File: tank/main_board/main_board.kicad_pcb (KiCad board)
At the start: 2 copper layers, 59.7 x 72.4 mm, 45 parts, among them J1 PowerIn, J10 Sonar2, J11 Programming Header, J12 SigOut, J13 Conn_01x01, J14 Conn_01x01, J15 Conn_01x01, J16 PowerOut, J2 Conn_01x01, J3 Conn_01x01, J4 LED, J5 Conn_01x01, J6 Spk, J7 Hall2, J8 Hall1, J9 Sonar1, Q1 2N3904, U1 LM317_TO3, U2 ATMEGA328P-PU, U3 SN754410, U4 SN754410, Y1 Crystal

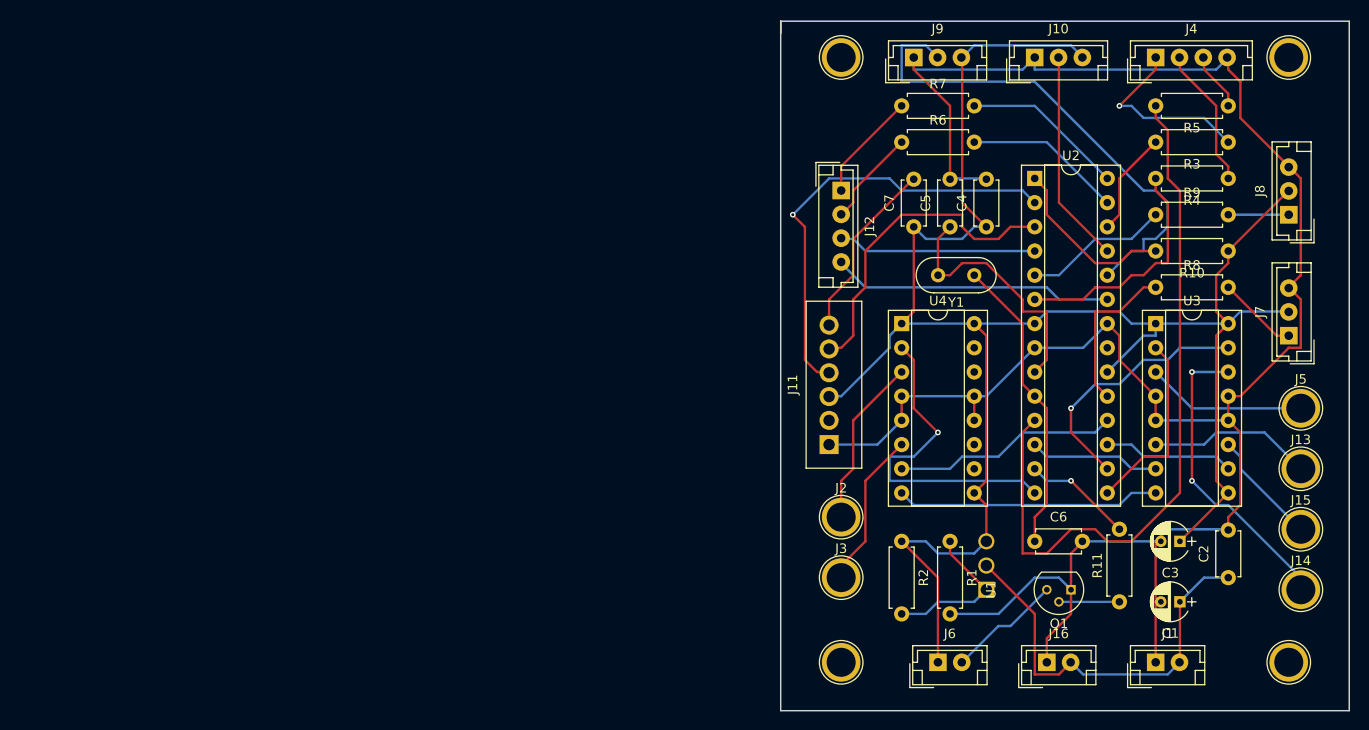
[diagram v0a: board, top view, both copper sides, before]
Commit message: Main Board v0.2
Adjustments to main board:
- resistors were inline when they shoulda been pull-ups
- adjust crystal footprint
- IR TX needs to be on pin 3
- silkscreen should have component names
- width of motor traces increased and added ground-fill
- motor vin isn't actually connected
- motor screw terminal footprints
- fix reset line - 1 uF cap
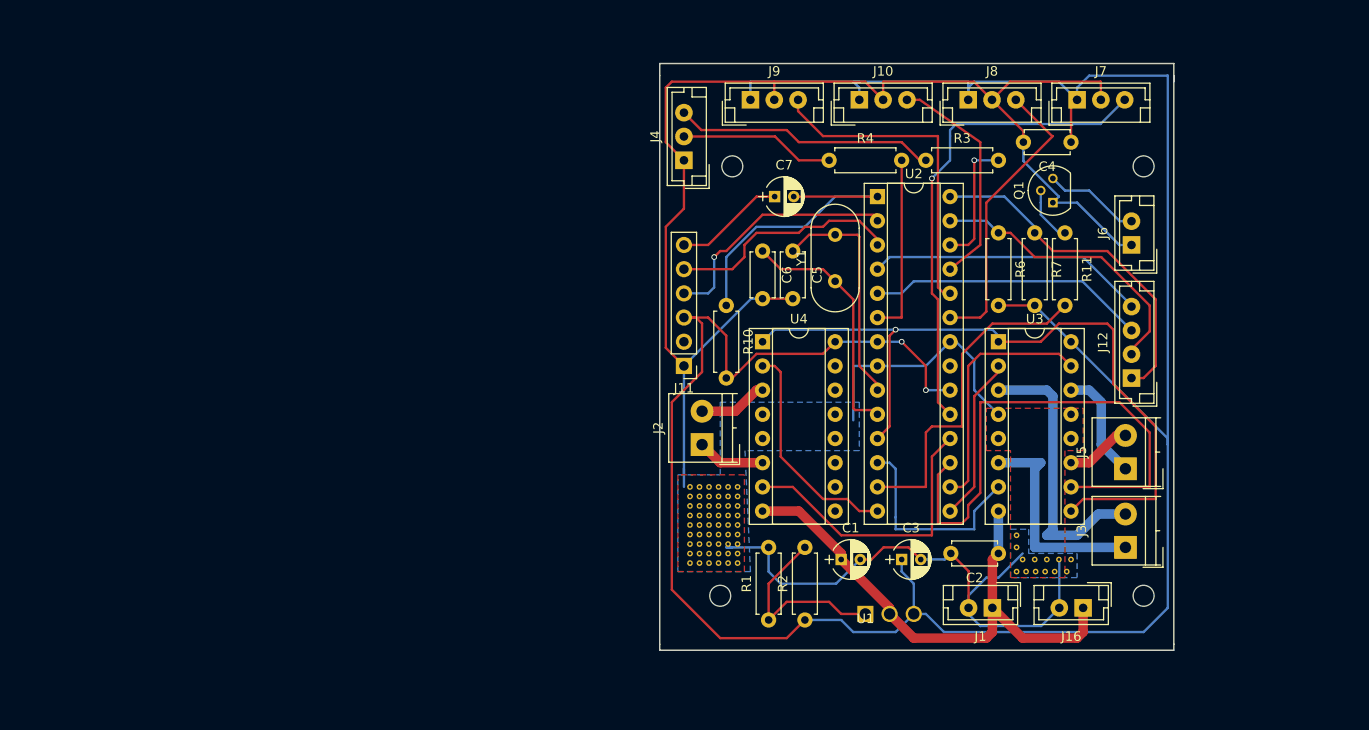
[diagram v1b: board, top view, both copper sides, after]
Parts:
- removed the G*** at (185.4, 130.8)
- removed J13, J14, J15: Conn_01x01, Connectors:1pin
- removed R5: R5, Resistors_THT:R_Axial_DIN0207_L6.3mm_D2.5mm_P7.62mm_Horizontal
- removed R8: R8, Resistors_THT:R_Axial_DIN0207_L6.3mm_D2.5mm_P7.62mm_Horizontal
- removed R9: R, Resistors_THT:R_Axial_DIN0207_L6.3mm_D2.5mm_P7.62mm_Horizontal
- removed the REF** at (176.5, 74.9)
- removed the REF** at (223.5, 74.9)
- removed the REF** at (223.5, 138.4)
- removed the REF** at (176.5, 138.4)
- added G***: LOGO, modules:miar_logo, B.Cu at (184.8, 113.0)
- added REF**: VIA-0.6mm, modules:VIA-0.6mm, F.Cu at (194.9, 126.4)
- added REF**: VIA-0.6mm, modules:VIA-0.6mm, F.Cu at (164.7, 127.0)
- added REF**: VIA-0.6mm, modules:VIA-0.6mm, F.Cu at (163.7, 127.0)
- added REF**: VIA-0.6mm, modules:VIA-0.6mm, F.Cu at (162.7, 127.0)
- added REF**: VIA-0.6mm, modules:VIA-0.6mm, F.Cu at (161.7, 127.0)
- added REF**: VIA-0.6mm, modules:VIA-0.6mm, F.Cu at (160.7, 127.0)
- added REF**: VIA-0.6mm, modules:VIA-0.6mm, F.Cu at (165.7, 126.0)
- added REF**: VIA-0.6mm, modules:VIA-0.6mm, F.Cu at (164.7, 126.0)
- added REF**: VIA-0.6mm, modules:VIA-0.6mm, F.Cu at (163.7, 126.0)
- added REF**: VIA-0.6mm, modules:VIA-0.6mm, F.Cu at (162.7, 126.0)
- added REF**: VIA-0.6mm, modules:VIA-0.6mm, F.Cu at (161.7, 126.0)
- added REF**: VIA-0.6mm, modules:VIA-0.6mm, F.Cu at (194.9, 125.1)
- added REF**: VIA-0.6mm, modules:VIA-0.6mm, F.Cu at (160.7, 126.0)
- added REF**: VIA-0.6mm, modules:VIA-0.6mm, F.Cu at (165.7, 125.0)
- added REF**: VIA-0.6mm, modules:VIA-0.6mm, F.Cu at (164.7, 125.0)
- added REF**: VIA-0.6mm, modules:VIA-0.6mm, F.Cu at (163.7, 125.0)
- added REF**: VIA-0.6mm, modules:VIA-0.6mm, F.Cu at (162.7, 125.0)
- added REF**: VIA-0.6mm, modules:VIA-0.6mm, F.Cu at (161.7, 125.0)
- added REF**: VIA-0.6mm, modules:VIA-0.6mm, F.Cu at (160.7, 125.0)
- added REF**: VIA-0.6mm, modules:VIA-0.6mm, F.Cu at (165.7, 124.0)
- added REF**: VIA-0.6mm, modules:VIA-0.6mm, F.Cu at (164.7, 124.0)
- added REF**: VIA-0.6mm, modules:VIA-0.6mm, F.Cu at (163.7, 124.0)
- added REF**: VIA-0.6mm, modules:VIA-0.6mm, F.Cu at (165.7, 128.0)
- added REF**: VIA-0.6mm, modules:VIA-0.6mm, F.Cu at (162.7, 124.0)
- added REF**: VIA-0.6mm, modules:VIA-0.6mm, F.Cu at (161.7, 124.0)
- added REF**: VIA-0.6mm, modules:VIA-0.6mm, F.Cu at (160.7, 124.0)
- added REF**: VIA-0.6mm, modules:VIA-0.6mm, F.Cu at (165.7, 123.0)
- added REF**: VIA-0.6mm, modules:VIA-0.6mm, F.Cu at (164.7, 123.0)
- added REF**: VIA-0.6mm, modules:VIA-0.6mm, F.Cu at (163.7, 123.0)
- added REF**: VIA-0.6mm, modules:VIA-0.6mm, F.Cu at (162.7, 123.0)
- added REF**: VIA-0.6mm, modules:VIA-0.6mm, F.Cu at (161.7, 123.0)
- added REF**: VIA-0.6mm, modules:VIA-0.6mm, F.Cu at (160.7, 123.0)
- added REF**: VIA-0.6mm, modules:VIA-0.6mm, F.Cu at (165.7, 122.0)
- added REF**: VIA-0.6mm, modules:VIA-0.6mm, F.Cu at (164.7, 128.0)
- added REF**: VIA-0.6mm, modules:VIA-0.6mm, F.Cu at (164.7, 122.0)
- added REF**: VIA-0.6mm, modules:VIA-0.6mm, F.Cu at (163.7, 122.0)
- added REF**: VIA-0.6mm, modules:VIA-0.6mm, F.Cu at (162.7, 122.0)
- added REF**: VIA-0.6mm, modules:VIA-0.6mm, F.Cu at (161.7, 122.0)
- added REF**: VIA-0.6mm, modules:VIA-0.6mm, F.Cu at (160.7, 122.0)
- added REF**: VIA-0.6mm, modules:VIA-0.6mm, F.Cu at (165.7, 121.0)
- added REF**: VIA-0.6mm, modules:VIA-0.6mm, F.Cu at (164.7, 121.0)
- added REF**: VIA-0.6mm, modules:VIA-0.6mm, F.Cu at (163.7, 121.0)
- added REF**: VIA-0.6mm, modules:VIA-0.6mm, F.Cu at (162.7, 121.0)
- added REF**: VIA-0.6mm, modules:VIA-0.6mm, F.Cu at (161.7, 121.0)
- added REF**: VIA-0.6mm, modules:VIA-0.6mm, F.Cu at (163.7, 128.0)
- added REF**: VIA-0.6mm, modules:VIA-0.6mm, F.Cu at (160.7, 121.0)
- added REF**: VIA-0.6mm, modules:VIA-0.6mm, F.Cu at (165.7, 120.0)
- added REF**: VIA-0.6mm, modules:VIA-0.6mm, F.Cu at (164.7, 120.0)
- added REF**: VIA-0.6mm, modules:VIA-0.6mm, F.Cu at (163.7, 120.0)
- added REF**: VIA-0.6mm, modules:VIA-0.6mm, F.Cu at (162.7, 120.0)
- added REF**: VIA-0.6mm, modules:VIA-0.6mm, F.Cu at (161.7, 120.0)
- added REF**: VIA-0.6mm, modules:VIA-0.6mm, F.Cu at (160.7, 120.0)
- added REF**: VIA-0.6mm, modules:VIA-0.6mm, F.Cu at (200.2, 128.9)
- added REF**: VIA-0.6mm, modules:VIA-0.6mm, F.Cu at (198.9, 128.9)
- added REF**: VIA-0.6mm, modules:VIA-0.6mm, F.Cu at (197.9, 128.9)
- added REF**: VIA-0.6mm, modules:VIA-0.6mm, F.Cu at (162.7, 128.0)
- added REF**: VIA-0.6mm, modules:VIA-0.6mm, F.Cu at (196.9, 128.9)
- added REF**: VIA-0.6mm, modules:VIA-0.6mm, F.Cu at (195.9, 128.9)
- added REF**: VIA-0.6mm, modules:VIA-0.6mm, F.Cu at (194.9, 128.9)
- added REF**: VIA-0.6mm, modules:VIA-0.6mm, F.Cu at (200.7, 127.6)
- added REF**: VIA-0.6mm, modules:VIA-0.6mm, F.Cu at (199.4, 127.6)
- added REF**: VIA-0.6mm, modules:VIA-0.6mm, F.Cu at (198.1, 127.6)
- added REF**: VIA-0.6mm, modules:VIA-0.6mm, F.Cu at (196.8, 127.6)
- added REF**: MountingHole_2.2mm_M2, Mounting_Holes:MountingHole_2.2mm_M2, F.Cu at (208.3, 131.4)
- added REF**: MountingHole_2.2mm_M2, Mounting_Holes:MountingHole_2.2mm_M2, F.Cu at (163.8, 131.4)
- added REF**: MountingHole_2.2mm_M2, Mounting_Holes:MountingHole_2.2mm_M2, F.Cu at (165.1, 86.4)
- added REF**: VIA-0.6mm, modules:VIA-0.6mm, F.Cu at (161.7, 128.0)
- added REF**: MountingHole_2.2mm_M2, Mounting_Holes:MountingHole_2.2mm_M2, F.Cu at (208.3, 86.4)
- added REF**: VIA-0.6mm, modules:VIA-0.6mm, F.Cu at (195.6, 127.6)
- added REF**: VIA-0.6mm, modules:VIA-0.6mm, F.Cu at (160.7, 128.0)
- added REF**: VIA-0.6mm, modules:VIA-0.6mm, F.Cu at (165.7, 127.0)
- C7: value C7 -> CP; footprint Capacitors_THT:C_Disc_D4.7mm_W2.5mm_P5.00mm -> Capacitors_THT:CP_Radial_D4.0mm_P2.00mm
- J1: value PowerIn -> Conn_01x02_Male
- J11: footprint Connectors:Wafer_Vertical17.5x5.8x7RM2.5-6 -> Pin_Headers:Pin_Header_Straight_1x06_Pitch2.54mm
- J2, J3, J5: value Conn_01x01 -> Conn_01x02; footprint Connectors:1pin -> Connectors_Terminal_Blocks:TerminalBlock_4UCON_19963_02x3.5mm_Straight
- J4: value LED -> Conn_01x03_Male; footprint JST:JST_EH_B04B-EH-A_04x2.50mm_Straight -> JST:JST_EH_B03B-EH-A_03x2.50mm_Straight
- Y1: footprint Crystals:Crystal_HC52-6mm_Vertical -> Crystals:Crystal_HC49-U_Vertical
- moved R10 53.0 mm to (164.5, 101.0), turned to 270 degrees
- moved J4 50.7 mm to (160.0, 85.7), turned to 90 degrees
- moved J6 48.3 mm to (207.0, 94.6), turned to 90 degrees
- moved R4 42.0 mm to (175.3, 85.7), turned to 0 degrees
- moved C6 41.8 mm to (168.3, 95.2), turned to 270 degrees
- moved Q1 40.7 mm to (198.8, 90.2), turned to 90 degrees
- moved R11 39.2 mm to (200.0, 93.3), turned to 270 degrees
- moved J12 36.3 mm to (207.0, 108.6), turned to 90 degrees
- moved C1 35.8 mm to (176.5, 127.6), turned to 0 degrees
- moved J8 35.8 mm to (189.9, 79.4), turned to 0 degrees
- moved J7 33.3 mm to (201.3, 79.4), turned to 0 degrees
- moved R3 31.8 mm to (185.4, 85.7), turned to 0 degrees
- moved J3 30.0 mm to (206.4, 126.4), turned to 90 degrees
- moved C3 29.3 mm to (182.9, 127.6), turned to 0 degrees
- moved C2 24.3 mm to (193.0, 127.0), turned to 180 degrees
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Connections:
- net LED2 renamed LED0
- net Speaker renamed SPK
- C1 pad 1: Net-(C1-Pad1) -> 5V
- C2 pad 1: Net-(C1-Pad1) -> 5V
- C7 pad 1: 4.5V -> Net-(C7-Pad1)
- J1 pad 1: GND -> 5V
- J1 pad 2: Net-(C1-Pad1) -> GND
- J10 pad 1: GND -> 4.5V
- J10 pad 2: Sonar2 -> GND
- J10 pad 3: 4.5V -> Net-(J10-Pad3)
- J11 pad 4: Net-(J11-Pad4) -> Rx
- J11 pad 5: Net-(J11-Pad5) -> Tx
- J11 pad 6: Net-(C7-Pad2) -> Net-(C7-Pad1)
- J12 pad 1: SLC -> SCL
- J12 pad 3: Rx -> IRTx
- J12 pad 4: Tx -> IRRx
- J16 pad 1: GND -> 5V
- J16 pad 2: Net-(C1-Pad1) -> GND
- J4 pad 1: Net-(J4-Pad1) -> GND
- J6 pad 1: 4.5V -> GND
- J7 pad 1: TurretCal -> 4.5V
- J7 pad 2: 4.5V -> GND
- J7 pad 3: GND -> Net-(J7-Pad3)
- J8 pad 1: TurretEnc -> 4.5V
- J8 pad 2: 4.5V -> GND
- J8 pad 3: GND -> Net-(J8-Pad3)
- J9 pad 1: GND -> 4.5V
- J9 pad 2: Sonar1 -> GND
- J9 pad 3: 4.5V -> Net-(J9-Pad3)
- R10 pad 1: 4.5V -> Net-(C7-Pad2)
- R10 pad 2: Net-(R10-Pad2) -> 4.5V
- R3 pad 1: Net-(J4-Pad1) -> Net-(J4-Pad3)
- R6 pad 2: Net-(R6-Pad2) -> 4.5V
- R7 pad 1: SLC -> SCL
- R7 pad 2: Net-(R7-Pad2) -> 4.5V
- U1 pad 2: Net-(C1-Pad1) -> 5V
- U2 pad 1: Net-(R10-Pad2) -> Net-(C7-Pad2)
- U2 pad 11: LED3 -> MEnable
- U2 pad 19: Net-(R8-Pad1) -> Net-(J7-Pad3)
- U2 pad 2: Net-(J11-Pad4) -> Rx
- U2 pad 23: Tx -> Net-(J8-Pad3)
- U2 pad 24: Sonar1 -> Net-(J9-Pad3)
- U2 pad 25: Sonar2 -> Net-(J10-Pad3)
- U2 pad 27: Net-(R6-Pad2) -> SDA
- U2 pad 28: Net-(R7-Pad2) -> SCL
- U2 pad 3: Net-(J11-Pad5) -> Tx
- U2 pad 4: Rx -> IRRx
- U2 pad 5: Net-(R9-Pad1) -> IRTx
- U3 pad 1: 4.5V -> MEnable
- U3 pad 11: Net-(J15-Pad1) -> Net-(J5-Pad2)
- U3 pad 14: Net-(J14-Pad1) -> Net-(J5-Pad1)
- U3 pad 3: Net-(J5-Pad1) -> Net-(J3-Pad2)
- U3 pad 6: Net-(J13-Pad1) -> Net-(J3-Pad1)
- U3 pad 9: 4.5V -> MEnable
- U4 pad 1: 4.5V -> MEnable
- U4 pad 3: Net-(J2-Pad1) -> Net-(J2-Pad2)
- U4 pad 6: Net-(J3-Pad1) -> Net-(J2-Pad1)
- U4 pad 9: 4.5V -> Net-(U4-Pad9)
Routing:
- net MEnable: track 0.00 -> 80.6 mm, vias 0 -> 1
- net LED3: track 76.4 -> 0.00 mm
- net 4.5V: track 206.3 -> 275.0 mm, vias 0 -> 2
- net Sonar1: track 53.1 -> 0.00 mm
- net Net-(J7-Pad3): track 0.00 -> 51.1 mm, vias 0 -> 1
- net Net-(J11-Pad4): track 46.9 -> 0.00 mm, vias 1 -> 0
- net Net-(C1-Pad1): track 43.0 -> 0.00 mm
- net M1-: track 13.8 -> 56.0 mm
- net SCL: track 0.00 -> 36.5 mm
- net Net-(J9-Pad3): track 0.00 -> 34.4 mm
- net Net-(J11-Pad5): track 34.3 -> 0.00 mm
- net Net-(J14-Pad1): track 32.1 -> 0.00 mm, vias 2 -> 0
- net Net-(J8-Pad3): track 0.00 -> 30.8 mm
- net IRTx: track 0.00 -> 30.5 mm
- net Net-(J3-Pad2): track 0.00 -> 30.0 mm
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- added copper zone on B.Cu, net GND
- added copper zone on F.Cu, net GND
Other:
- board size 59.7 x 72.4 mm -> 54 x 61.6 mm
- net class Motor: clearance 0.4 -> 0.2; trace_width 0.5 -> 1
- board text added: "Laser Tag Robot Tank Main Board v0.2 M.I.A.R. Labs nick.groesz@gmail.com"
- board text removed: "Tank Main Board v0.1 M.I.A.R Labs nick.groesz@gmail.com"

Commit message: Main Board v0.3 - changed motor controllers to TB6612FNG - changed speaker transistor wiring - supports 4 LEDs, using switched ground
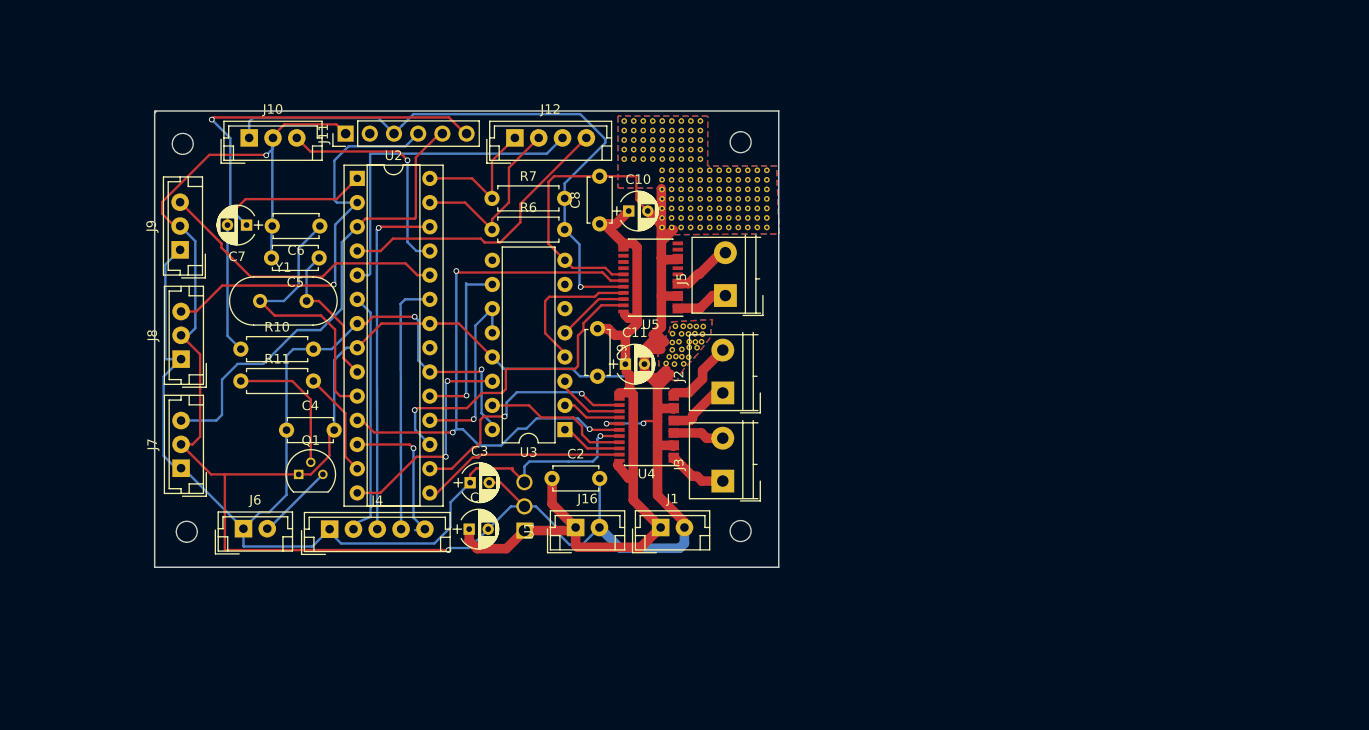
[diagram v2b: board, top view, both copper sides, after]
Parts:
- removed the G*** at (184.8, 113.0)
- removed R1: R1, Resistors_THT:R_Axial_DIN0207_L6.3mm_D2.5mm_P7.62mm_Horizontal
- removed R2: R2, Resistors_THT:R_Axial_DIN0207_L6.3mm_D2.5mm_P7.62mm_Horizontal
- removed R3: R3, Resistors_THT:R_Axial_DIN0207_L6.3mm_D2.5mm_P7.62mm_Horizontal
- removed R4: R4, Resistors_THT:R_Axial_DIN0207_L6.3mm_D2.5mm_P7.62mm_Horizontal
- removed the REF** at (194.9, 126.4)
- removed the REF** at (164.7, 127.0)
- removed the REF** at (163.7, 127.0)
- removed the REF** at (162.7, 127.0)
- removed the REF** at (161.7, 127.0)
- removed the REF** at (160.7, 127.0)
- removed the REF** at (165.7, 126.0)
- removed the REF** at (164.7, 126.0)
- removed the REF** at (163.7, 126.0)
- removed the REF** at (162.7, 126.0)
- removed the REF** at (161.7, 126.0)
- removed the REF** at (194.9, 125.1)
- removed the REF** at (160.7, 126.0)
- removed the REF** at (165.7, 125.0)
- removed the REF** at (164.7, 125.0)
- removed the REF** at (163.7, 125.0)
- removed the REF** at (162.7, 125.0)
- removed the REF** at (161.7, 125.0)
- removed the REF** at (160.7, 125.0)
- removed the REF** at (165.7, 124.0)
- removed the REF** at (164.7, 124.0)
- removed the REF** at (163.7, 124.0)
- removed the REF** at (165.7, 128.0)
- removed the REF** at (162.7, 124.0)
- removed the REF** at (161.7, 124.0)
- removed the REF** at (160.7, 124.0)
- removed the REF** at (165.7, 123.0)
- removed the REF** at (164.7, 123.0)
- removed the REF** at (163.7, 123.0)
- removed the REF** at (162.7, 123.0)
- removed the REF** at (161.7, 123.0)
- removed the REF** at (160.7, 123.0)
- removed the REF** at (165.7, 122.0)
- removed the REF** at (164.7, 128.0)
- removed the REF** at (164.7, 122.0)
- removed the REF** at (163.7, 122.0)
- removed the REF** at (162.7, 122.0)
- removed the REF** at (161.7, 122.0)
- removed the REF** at (160.7, 122.0)
- removed the REF** at (165.7, 121.0)
- removed the REF** at (164.7, 121.0)
- removed the REF** at (163.7, 121.0)
- removed the REF** at (162.7, 121.0)
- removed the REF** at (161.7, 121.0)
- removed the REF** at (163.7, 128.0)
- removed the REF** at (160.7, 121.0)
- removed the REF** at (165.7, 120.0)
- removed the REF** at (164.7, 120.0)
- removed the REF** at (163.7, 120.0)
- removed the REF** at (162.7, 120.0)
- removed the REF** at (161.7, 120.0)
- removed the REF** at (160.7, 120.0)
- removed the REF** at (200.2, 128.9)
- removed the REF** at (198.9, 128.9)
- removed the REF** at (197.9, 128.9)
- removed the REF** at (162.7, 128.0)
- removed the REF** at (196.9, 128.9)
- removed the REF** at (195.9, 128.9)
- removed the REF** at (194.9, 128.9)
- removed the REF** at (200.7, 127.6)
- removed the REF** at (199.4, 127.6)
- removed the REF** at (198.1, 127.6)
- removed the REF** at (196.8, 127.6)
- removed the REF** at (208.3, 131.4)
- removed the REF** at (163.8, 131.4)
- removed the REF** at (165.1, 86.4)
- removed the REF** at (161.7, 128.0)
- removed the REF** at (208.3, 86.4)
- removed the REF** at (195.6, 127.6)
- removed the REF** at (160.7, 128.0)
- removed the REF** at (165.7, 127.0)
- added C10: CP, Capacitors_THT:CP_Radial_D4.0mm_P2.00mm, F.Cu at (154.2, 91.0)
- added C11: CP, Capacitors_THT:CP_Radial_D4.0mm_P2.00mm, F.Cu at (153.9, 107.1)
- added C8: C, Capacitors_THT:C_Disc_D4.7mm_W2.5mm_P5.00mm, F.Cu at (151.2, 92.4)
- added C9: C, Capacitors_THT:C_Disc_D4.7mm_W2.5mm_P5.00mm, F.Cu at (150.9, 103.4)
- added G***: LOGO, modules:Tank, B.Cu at (129.2, 115.0)
- added REF**: VIA-0.6mm, modules:VIA-0.6mm, F.Cu at (158.2, 107.0)
- added REF**: VIA-0.6mm, modules:VIA-0.6mm, F.Cu at (160.6, 105.4)
- added REF**: VIA-0.6mm, modules:VIA-0.6mm, F.Cu at (166.7, 86.8)
- added REF**: VIA-0.6mm, modules:VIA-0.6mm, F.Cu at (165.7, 86.8)
- added REF**: VIA-0.6mm, modules:VIA-0.6mm, F.Cu at (164.7, 86.8)
- added REF**: VIA-0.6mm, modules:VIA-0.6mm, F.Cu at (163.7, 86.8)
- added REF**: VIA-0.6mm, modules:VIA-0.6mm, F.Cu at (162.7, 86.8)
- added REF**: VIA-0.6mm, modules:VIA-0.6mm, F.Cu at (161.7, 86.8)
- added REF**: VIA-0.6mm, modules:VIA-0.6mm, F.Cu at (160.7, 86.8)
- added REF**: VIA-0.6mm, modules:VIA-0.6mm, F.Cu at (159.7, 86.8)
- added REF**: VIA-0.6mm, modules:VIA-0.6mm, F.Cu at (158.7, 86.8)
- added REF**: VIA-0.6mm, modules:VIA-0.6mm, F.Cu at (157.7, 86.8)
- added REF**: VIA-0.6mm, modules:VIA-0.6mm, F.Cu at (161.4, 105.4)
- added REF**: VIA-0.6mm, modules:VIA-0.6mm, F.Cu at (161.8, 85.6)
- added REF**: VIA-0.6mm, modules:VIA-0.6mm, F.Cu at (160.8, 85.6)
- added REF**: VIA-0.6mm, modules:VIA-0.6mm, F.Cu at (159.8, 85.6)
- added REF**: VIA-0.6mm, modules:VIA-0.6mm, F.Cu at (158.8, 85.6)
- added REF**: VIA-0.6mm, modules:VIA-0.6mm, F.Cu at (157.8, 85.6)
- added REF**: VIA-0.6mm, modules:VIA-0.6mm, F.Cu at (156.8, 85.6)
- added REF**: VIA-0.6mm, modules:VIA-0.6mm, F.Cu at (155.8, 85.6)
- added REF**: VIA-0.6mm, modules:VIA-0.6mm, F.Cu at (154.8, 85.6)
- added REF**: VIA-0.6mm, modules:VIA-0.6mm, F.Cu at (153.8, 85.6)
- added REF**: VIA-0.6mm, modules:VIA-0.6mm, F.Cu at (161.8, 84.6)
- added REF**: VIA-0.6mm, modules:VIA-0.6mm, F.Cu at (161.9, 104.8)
- added REF**: VIA-0.6mm, modules:VIA-0.6mm, F.Cu at (160.8, 84.6)
- added REF**: VIA-0.6mm, modules:VIA-0.6mm, F.Cu at (159.8, 84.6)
- added REF**: VIA-0.6mm, modules:VIA-0.6mm, F.Cu at (158.8, 84.6)
- added REF**: VIA-0.6mm, modules:VIA-0.6mm, F.Cu at (157.8, 84.6)
- added REF**: VIA-0.6mm, modules:VIA-0.6mm, F.Cu at (156.8, 84.6)
- added REF**: VIA-0.6mm, modules:VIA-0.6mm, F.Cu at (155.8, 84.6)
- added REF**: VIA-0.6mm, modules:VIA-0.6mm, F.Cu at (154.8, 84.6)
- added REF**: VIA-0.6mm, modules:VIA-0.6mm, F.Cu at (153.8, 84.6)
- added REF**: VIA-0.6mm, modules:VIA-0.6mm, F.Cu at (161.8, 83.6)
- added REF**: VIA-0.6mm, modules:VIA-0.6mm, F.Cu at (160.8, 83.6)
- added REF**: VIA-0.6mm, modules:VIA-0.6mm, F.Cu at (161.2, 104.8)
- added REF**: VIA-0.6mm, modules:VIA-0.6mm, F.Cu at (159.8, 83.6)
- added REF**: VIA-0.6mm, modules:VIA-0.6mm, F.Cu at (158.8, 83.6)
- added REF**: VIA-0.6mm, modules:VIA-0.6mm, F.Cu at (157.8, 83.6)
- added REF**: VIA-0.6mm, modules:VIA-0.6mm, F.Cu at (156.8, 83.6)
- added REF**: VIA-0.6mm, modules:VIA-0.6mm, F.Cu at (155.8, 83.6)
- added REF**: VIA-0.6mm, modules:VIA-0.6mm, F.Cu at (154.8, 83.6)
- added REF**: VIA-0.6mm, modules:VIA-0.6mm, F.Cu at (153.8, 83.6)
- added REF**: VIA-0.6mm, modules:VIA-0.6mm, F.Cu at (161.8, 82.6)
- added REF**: VIA-0.6mm, modules:VIA-0.6mm, F.Cu at (160.8, 82.6)
- added REF**: VIA-0.6mm, modules:VIA-0.6mm, F.Cu at (159.8, 82.6)
- added REF**: VIA-0.6mm, modules:VIA-0.6mm, F.Cu at (160.6, 104.8)
- added REF**: VIA-0.6mm, modules:VIA-0.6mm, F.Cu at (158.8, 82.6)
- added REF**: VIA-0.6mm, modules:VIA-0.6mm, F.Cu at (157.8, 82.6)
- added REF**: VIA-0.6mm, modules:VIA-0.6mm, F.Cu at (156.8, 82.6)
- added REF**: VIA-0.6mm, modules:VIA-0.6mm, F.Cu at (155.8, 82.6)
- added REF**: VIA-0.6mm, modules:VIA-0.6mm, F.Cu at (154.8, 82.6)
- added REF**: VIA-0.6mm, modules:VIA-0.6mm, F.Cu at (153.8, 82.6)
- added REF**: VIA-0.6mm, modules:VIA-0.6mm, F.Cu at (161.8, 81.6)
- added REF**: VIA-0.6mm, modules:VIA-0.6mm, F.Cu at (160.8, 81.6)
- added REF**: VIA-0.6mm, modules:VIA-0.6mm, F.Cu at (159.8, 81.6)
- added REF**: VIA-0.6mm, modules:VIA-0.6mm, F.Cu at (158.8, 81.6)
- added REF**: VIA-0.6mm, modules:VIA-0.6mm, F.Cu at (159.5, 104.8)
- added REF**: VIA-0.6mm, modules:VIA-0.6mm, F.Cu at (157.8, 81.6)
- added REF**: VIA-0.6mm, modules:VIA-0.6mm, F.Cu at (156.8, 81.6)
- added REF**: VIA-0.6mm, modules:VIA-0.6mm, F.Cu at (155.8, 81.6)
- added REF**: VIA-0.6mm, modules:VIA-0.6mm, F.Cu at (154.8, 81.6)
- added REF**: MountingHole_2.2mm_M2, Mounting_Holes:MountingHole_2.2mm_M2, F.Cu at (107.8, 124.7)
- added REF**: MountingHole_2.2mm_M2, Mounting_Holes:MountingHole_2.2mm_M2, F.Cu at (107.4, 84.0)
- added REF**: MountingHole_2.2mm_M2, Mounting_Holes:MountingHole_2.2mm_M2, F.Cu at (166.0, 83.8)
- added REF**: MountingHole_2.2mm_M2, Mounting_Holes:MountingHole_2.2mm_M2, F.Cu at (166.0, 124.7)
- added REF**: VIA-0.6mm, modules:VIA-0.6mm, F.Cu at (153.8, 81.6)
- added REF**: VIA-0.6mm, modules:VIA-0.6mm, F.Cu at (159.1, 103.2)
- added REF**: VIA-0.6mm, modules:VIA-0.6mm, F.Cu at (158.8, 104.8)
- added REF**: VIA-0.6mm, modules:VIA-0.6mm, F.Cu at (158.8, 103.9)
- added REF**: VIA-0.6mm, modules:VIA-0.6mm, F.Cu at (159.8, 104.0)
- added REF**: VIA-0.6mm, modules:VIA-0.6mm, F.Cu at (160.5, 104.0)
- added REF**: VIA-0.6mm, modules:VIA-0.6mm, F.Cu at (159.0, 107.1)
- added REF**: VIA-0.6mm, modules:VIA-0.6mm, F.Cu at (161.2, 103.9)
- added REF**: VIA-0.6mm, modules:VIA-0.6mm, F.Cu at (162.0, 104.0)
- added REF**: VIA-0.6mm, modules:VIA-0.6mm, F.Cu at (162.1, 103.2)
- added REF**: VIA-0.6mm, modules:VIA-0.6mm, F.Cu at (161.3, 103.2)
- added REF**: VIA-0.6mm, modules:VIA-0.6mm, F.Cu at (160.7, 103.2)
- added REF**: VIA-0.6mm, modules:VIA-0.6mm, F.Cu at (159.9, 103.2)
- added REF**: VIA-0.6mm, modules:VIA-0.6mm, F.Cu at (168.7, 92.8)
- added REF**: VIA-0.6mm, modules:VIA-0.6mm, F.Cu at (167.7, 92.8)
- added REF**: VIA-0.6mm, modules:VIA-0.6mm, F.Cu at (166.7, 92.8)
- added REF**: VIA-0.6mm, modules:VIA-0.6mm, F.Cu at (165.7, 92.8)
- added REF**: VIA-0.6mm, modules:VIA-0.6mm, F.Cu at (160.0, 107.1)
- added REF**: VIA-0.6mm, modules:VIA-0.6mm, F.Cu at (164.7, 92.8)
- added REF**: VIA-0.6mm, modules:VIA-0.6mm, F.Cu at (163.7, 92.8)
- added REF**: VIA-0.6mm, modules:VIA-0.6mm, F.Cu at (162.7, 92.8)
- added REF**: VIA-0.6mm, modules:VIA-0.6mm, F.Cu at (161.7, 92.8)
- added REF**: VIA-0.6mm, modules:VIA-0.6mm, F.Cu at (160.7, 92.8)
- added REF**: VIA-0.6mm, modules:VIA-0.6mm, F.Cu at (159.7, 92.8)
- added REF**: VIA-0.6mm, modules:VIA-0.6mm, F.Cu at (158.7, 92.8)
- added REF**: VIA-0.6mm, modules:VIA-0.6mm, F.Cu at (157.7, 92.8)
- added REF**: VIA-0.6mm, modules:VIA-0.6mm, F.Cu at (168.7, 91.8)
- added REF**: VIA-0.6mm, modules:VIA-0.6mm, F.Cu at (167.7, 91.8)
- added REF**: VIA-0.6mm, modules:VIA-0.6mm, F.Cu at (160.5, 106.4)
- added REF**: VIA-0.6mm, modules:VIA-0.6mm, F.Cu at (166.7, 91.8)
- added REF**: VIA-0.6mm, modules:VIA-0.6mm, F.Cu at (165.7, 91.8)
- added REF**: VIA-0.6mm, modules:VIA-0.6mm, F.Cu at (164.7, 91.8)
- added REF**: VIA-0.6mm, modules:VIA-0.6mm, F.Cu at (163.7, 91.8)
- added REF**: VIA-0.6mm, modules:VIA-0.6mm, F.Cu at (162.7, 91.8)
- added REF**: VIA-0.6mm, modules:VIA-0.6mm, F.Cu at (161.7, 91.8)
- added REF**: VIA-0.6mm, modules:VIA-0.6mm, F.Cu at (160.7, 91.8)
- added REF**: VIA-0.6mm, modules:VIA-0.6mm, F.Cu at (159.7, 91.8)
- added REF**: VIA-0.6mm, modules:VIA-0.6mm, F.Cu at (158.7, 91.8)
- added REF**: VIA-0.6mm, modules:VIA-0.6mm, F.Cu at (157.7, 91.8)
- added REF**: VIA-0.6mm, modules:VIA-0.6mm, F.Cu at (159.8, 106.3)
- added REF**: VIA-0.6mm, modules:VIA-0.6mm, F.Cu at (168.7, 90.8)
- added REF**: VIA-0.6mm, modules:VIA-0.6mm, F.Cu at (167.7, 90.8)
- added REF**: VIA-0.6mm, modules:VIA-0.6mm, F.Cu at (166.7, 90.8)
- added REF**: VIA-0.6mm, modules:VIA-0.6mm, F.Cu at (165.7, 90.8)
- added REF**: VIA-0.6mm, modules:VIA-0.6mm, F.Cu at (164.7, 90.8)
- added REF**: VIA-0.6mm, modules:VIA-0.6mm, F.Cu at (163.7, 90.8)
- added REF**: VIA-0.6mm, modules:VIA-0.6mm, F.Cu at (162.7, 90.8)
- added REF**: VIA-0.6mm, modules:VIA-0.6mm, F.Cu at (161.7, 90.8)
- added REF**: VIA-0.6mm, modules:VIA-0.6mm, F.Cu at (160.7, 90.8)
- added REF**: VIA-0.6mm, modules:VIA-0.6mm, F.Cu at (159.7, 90.8)
- added REF**: VIA-0.6mm, modules:VIA-0.6mm, F.Cu at (159.2, 106.3)
- added REF**: VIA-0.6mm, modules:VIA-0.6mm, F.Cu at (158.7, 90.8)
- added REF**: VIA-0.6mm, modules:VIA-0.6mm, F.Cu at (157.7, 90.8)
- added REF**: VIA-0.6mm, modules:VIA-0.6mm, F.Cu at (168.7, 89.8)
- added REF**: VIA-0.6mm, modules:VIA-0.6mm, F.Cu at (167.7, 89.8)
- added REF**: VIA-0.6mm, modules:VIA-0.6mm, F.Cu at (166.7, 89.8)
- added REF**: VIA-0.6mm, modules:VIA-0.6mm, F.Cu at (165.7, 89.8)
- added REF**: VIA-0.6mm, modules:VIA-0.6mm, F.Cu at (164.7, 89.8)
- added REF**: VIA-0.6mm, modules:VIA-0.6mm, F.Cu at (163.7, 89.8)
- added REF**: VIA-0.6mm, modules:VIA-0.6mm, F.Cu at (162.7, 89.8)
- added REF**: VIA-0.6mm, modules:VIA-0.6mm, F.Cu at (161.7, 89.8)
- added REF**: VIA-0.6mm, modules:VIA-0.6mm, F.Cu at (158.5, 106.3)
- added REF**: VIA-0.6mm, modules:VIA-0.6mm, F.Cu at (160.7, 89.8)
- added REF**: VIA-0.6mm, modules:VIA-0.6mm, F.Cu at (159.7, 89.8)
- added REF**: VIA-0.6mm, modules:VIA-0.6mm, F.Cu at (158.7, 89.8)
- added REF**: VIA-0.6mm, modules:VIA-0.6mm, F.Cu at (157.7, 89.8)
- added REF**: VIA-0.6mm, modules:VIA-0.6mm, F.Cu at (168.7, 88.8)
- added REF**: VIA-0.6mm, modules:VIA-0.6mm, F.Cu at (167.7, 88.8)
- added REF**: VIA-0.6mm, modules:VIA-0.6mm, F.Cu at (166.7, 88.8)
- added REF**: VIA-0.6mm, modules:VIA-0.6mm, F.Cu at (165.7, 88.8)
- added REF**: VIA-0.6mm, modules:VIA-0.6mm, F.Cu at (164.7, 88.8)
- added REF**: VIA-0.6mm, modules:VIA-0.6mm, F.Cu at (163.7, 88.8)
- added REF**: VIA-0.6mm, modules:VIA-0.6mm, F.Cu at (158.8, 105.6)
- added REF**: VIA-0.6mm, modules:VIA-0.6mm, F.Cu at (162.7, 88.8)
- added REF**: VIA-0.6mm, modules:VIA-0.6mm, F.Cu at (161.7, 88.8)
- added REF**: VIA-0.6mm, modules:VIA-0.6mm, F.Cu at (160.7, 88.8)
- added REF**: VIA-0.6mm, modules:VIA-0.6mm, F.Cu at (159.7, 88.8)
- added REF**: VIA-0.6mm, modules:VIA-0.6mm, F.Cu at (158.7, 88.8)
- added REF**: VIA-0.6mm, modules:VIA-0.6mm, F.Cu at (157.7, 88.8)
- added REF**: VIA-0.6mm, modules:VIA-0.6mm, F.Cu at (168.7, 87.8)
- added REF**: VIA-0.6mm, modules:VIA-0.6mm, F.Cu at (167.7, 87.8)
- added REF**: VIA-0.6mm, modules:VIA-0.6mm, F.Cu at (166.7, 87.8)
- added REF**: VIA-0.6mm, modules:VIA-0.6mm, F.Cu at (165.7, 87.8)
- added REF**: VIA-0.6mm, modules:VIA-0.6mm, F.Cu at (159.8, 105.6)
- added REF**: VIA-0.6mm, modules:VIA-0.6mm, F.Cu at (164.7, 87.8)
- added REF**: VIA-0.6mm, modules:VIA-0.6mm, F.Cu at (163.7, 87.8)
- added REF**: VIA-0.6mm, modules:VIA-0.6mm, F.Cu at (162.7, 87.8)
- added REF**: VIA-0.6mm, modules:VIA-0.6mm, F.Cu at (161.7, 87.8)
- added REF**: VIA-0.6mm, modules:VIA-0.6mm, F.Cu at (160.7, 87.8)
- added REF**: VIA-0.6mm, modules:VIA-0.6mm, F.Cu at (159.7, 87.8)
- added REF**: VIA-0.6mm, modules:VIA-0.6mm, F.Cu at (158.7, 87.8)
- added REF**: VIA-0.6mm, modules:VIA-0.6mm, F.Cu at (157.7, 87.8)
- added REF**: VIA-0.6mm, modules:VIA-0.6mm, F.Cu at (168.7, 86.8)
- added REF**: VIA-0.6mm, modules:VIA-0.6mm, F.Cu at (167.7, 86.8)
- added U5: TB6612FNG, Custom:TB6612FNGSINGLE, F.Cu at (156.5, 98.0)
- J2, J3, J5: footprint Connectors_Terminal_Blocks:TerminalBlock_4UCON_19963_02x3.5mm_Straight -> Custom:TerminalBlock_4UCON_19963_02x4.5mm_Straight
- J4: value Conn_01x03_Male -> Conn_01x05; footprint JST:JST_EH_B03B-EH-A_03x2.50mm_Straight -> Connectors_JST:JST_EH_B05B-EH-A_05x2.50mm_Straight
- U1: value LM317_TO3 -> L7805; footprint Custom:LM317T -> Custom:L7805
- U3: value SN754410 -> SN74HC595; footprint Housings_DIP:DIP-16_W7.62mm_Socket -> Housings_DIP:DIP-16_W7.62mm
- U4: value SN754410 -> TB6612FNG; footprint Housings_DIP:DIP-16_W7.62mm_Socket -> Custom:TB6612FNG
- moved J7 101.7 mm to (107.2, 118.0), turned to 90 degrees
- moved J6 97.9 mm to (113.8, 124.4), turned to 0 degrees
- moved R11 87.9 mm to (113.5, 108.9), turned to 0 degrees
- moved C4 87.7 mm to (118.3, 114.0), turned to 0 degrees
- moved J8 87.0 mm to (107.2, 106.6), turned to 90 degrees
- moved Q1 84.2 mm to (119.6, 118.7), turned to 0 degrees
- moved J12 69.5 mm to (142.3, 83.4), turned to 0 degrees
- moved J10 64.2 mm to (114.4, 83.4)
- moved J9 61.9 mm to (107.1, 95.1), turned to 90 degrees
- moved Y1 60.4 mm to (115.5, 100.5), turned to 0 degrees
- moved R7 57.1 mm to (139.9, 89.7), turned to 0 degrees
- moved C7 55.5 mm to (114.1, 92.5), turned to 180 degrees
- moved U2 54.6 mm to (125.7, 87.6)
- moved J16 53.9 mm to (148.7, 124.3), turned to 0 degrees
- moved J4 53.7 mm to (122.8, 124.5), turned to 0 degrees
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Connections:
- net Net-(J10-Pad3) renamed Sonar1
- net Net-(J9-Pad3) renamed Sonar0
- J11 pad 4: Rx -> Hall0
- J11 pad 5: Tx -> Hall1
- J4 pad 1: GND -> 4.5V
- J4 pad 2: Net-(J4-Pad2) -> LED0
- J4 pad 3: Net-(J4-Pad3) -> LED1
- J6 pad 1: GND -> 4.5V
- J7 pad 3: Net-(J7-Pad3) -> Hall1
- J8 pad 3: Net-(J8-Pad3) -> Hall0
- U1 pad 1: Net-(R1-Pad1) -> 5V
- U1 pad 2: 5V -> GND
- U2 pad 12: M0- -> LED3
- U2 pad 14: M2+ -> SER
- U2 pad 15: M0+ -> M0PWM
- U2 pad 16: M1+ -> M1PWM
- U2 pad 17: M1- -> M2PWM
- U2 pad 18: M2- -> SRCLK
- U2 pad 19: Net-(J7-Pad3) -> SRCLR
- U2 pad 2: Rx -> Hall0
- U2 pad 23: Net-(J8-Pad3) -> LED2
- U2 pad 3: Tx -> Hall1
- U3 pad 1: MEnable -> M0-
- U3 pad 10: M1- -> SRCLR
- U3 pad 11: Net-(J5-Pad2) -> SRCLK
- U3 pad 12: GND -> SRCLK
- U3 pad 14: Net-(J5-Pad1) -> SER
- U3 pad 15: M1+ -> M0+
- U3 pad 2: M0+ -> M1+
- U3 pad 3: Net-(J3-Pad2) -> M1-
- U3 pad 4: GND -> M2+
- U3 pad 5: GND -> M2-
- U3 pad 6: Net-(J3-Pad1) -> Net-(U3-Pad6)
- U3 pad 7: M0- -> Net-(U3-Pad7)
- U3 pad 8: 5V -> GND
- U3 pad 9: MEnable -> Net-(U3-Pad9)
- U4 pad 1: MEnable -> Net-(J3-Pad1)
- U4 pad 10: Net-(U4-Pad10) -> GND
- U4 pad 11: Net-(U4-Pad11) -> Net-(J2-Pad2)
- U4 pad 12: GND -> Net-(J2-Pad2)
- U4 pad 13: GND -> 5V
- U4 pad 14: Net-(U4-Pad14) -> 5V
- U4 pad 15: Net-(U4-Pad15) -> M1PWM
- U4 pad 16: 4.5V -> M1-
- U4 pad 2: M2+ -> Net-(J3-Pad1)
- U4 pad 3: Net-(J2-Pad2) -> GND
- U4 pad 5: GND -> Net-(J3-Pad2)
- U4 pad 6: Net-(J2-Pad1) -> Net-(J3-Pad2)
- U4 pad 7: M2- -> Net-(J2-Pad1)
- U4 pad 8: 5V -> Net-(J2-Pad1)
- U4 pad 9: Net-(U4-Pad9) -> GND
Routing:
- net GND: track 226.5 -> 298.7 mm, vias 0 -> 4
- net 4.5V: track 275.0 -> 208.1 mm, vias 2 -> 4
- net Net-(J7-Pad3): track 51.1 -> 0.00 mm, vias 1 -> 0
- net Hall1: track 0.00 -> 49.9 mm
- net M1-: track 56.0 -> 7.42 mm
- net Hall0: track 0.00 -> 43.5 mm, vias 0 -> 1
- net M2PWM: track 0.00 -> 34.3 mm, vias 0 -> 1
- net Net-(J8-Pad3): track 30.8 -> 0.00 mm
- net Net-(C7-Pad1): track 11.6 -> 40.1 mm, vias 0 -> 1
- net Net-(J4-Pad3): track 27.5 -> 0.00 mm
- net LED2: track 0.00 -> 26.9 mm
- net M1PWM: track 0.00 -> 26.0 mm, vias 0 -> 2
- net Rx: track 25.9 -> 0.00 mm, vias 1 -> 0
- net Net-(J3-Pad2): track 30.0 -> 4.73 mm
- net SPK: track 36.0 -> 11.1 mm
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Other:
- board size 54 x 61.6 mm -> 65.5 x 47.9 mm
- net class Motor: clearance 0.2 -> 0.1524
- board text added: "Laser Tag Robot Tank Main Board v0.3 M.I.A.R. Labs nick.groesz@gmail.com"
- board text removed: "Laser Tag Robot Tank Main Board v0.2 M.I.A.R. Labs nick.groesz@gmail.com"

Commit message: Main Board v0.4
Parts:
- removed the REF** at (168.7, 92.8)
- removed the REF** at (167.7, 92.8)
- removed the REF** at (166.7, 92.8)
- removed the REF** at (165.7, 92.8)
- removed the REF** at (164.7, 92.8)
- removed the REF** at (163.7, 92.8)
- removed the REF** at (162.7, 92.8)
- removed the REF** at (161.7, 92.8)
- J1: value Conn_01x02_Male -> PowerIn
- J2: value Conn_01x02 -> M2
- J3: value Conn_01x02 -> M1
- J4: value Conn_01x05 -> LEDs
- J5: value Conn_01x02 -> M3
- moved G*** 33.3 mm to (151.8, 90.5), turned to 180 degrees
- moved J5 1.21 mm to (164.8, 98.8)
- moved U4 1.00 mm to (157.1, 113.7)
- moved J2 0.96 mm to (164.6, 109.3)
- moved J3 0.92 mm to (164.5, 120.2)
- moved U5 0.60 mm to (157.1, 98.0)
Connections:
- J4 pad 1: 4.5V -> 5V
- J6 pad 1: 4.5V -> 5V
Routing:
- net 4.5V: track 208.1 -> 171.9 mm, vias 4 -> 5
- net 5V: track 79.0 -> 106.7 mm
- net (no net): track 0.00 -> 6.14 mm
- net Net-(J5-Pad2): track 5.77 -> 0.00 mm
- net GND: track 298.7 -> 303.1 mm
- net Net-(J2-Pad2): track 7.53 -> 5.96 mm
- net Net-(J3-Pad1): track 6.11 -> 4.57 mm
- net Net-(J2-Pad1): track 5.98 -> 5.32 mm
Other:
- board size 65.5 x 47.9 mm -> 66.5 x 49.9 mm
- board text added: "GND NC 5V Rx Tx RST"
- board text added: "Laser Tag Robot Tank Main Board v0.4 M.I.A.R. Labs nick.groesz@gmail.com"
- board text removed: "Laser Tag Robot Tank Main Board v0.3 M.I.A.R. Labs nick.groesz@gmail.com"

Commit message: shut er down
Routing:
- net 4.5V: track 171.9 -> 179.8 mm, vias 5 -> 6
- net Net-(J5-Pad2): track 0.00 -> 7.07 mm
- net (no net): track 6.14 -> 0.00 mm
- net Net-(J3-Pad1): track 4.57 -> 6.24 mm
- net LED3: track 16.3 -> 15.1 mm
- net Net-(J2-Pad2): track 5.96 -> 7.23 mm
- net Net-(J2-Pad1): track 5.32 -> 6.24 mm
- net Net-(J3-Pad2): track 4.36 -> 5.07 mm
